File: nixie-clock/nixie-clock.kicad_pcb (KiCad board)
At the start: 2 copper layers, 184 x 112 mm, 61 parts, among them J1 Barrel_Jack_Switch, J2 Conn_01x08, J3 Conn_01x06, J4 AVR-ISP-6, SW1 SW_Push, SW2 SW_Push, SW3 SW_Push, SW4 SW_Push, U1 NCH6100HV, U10 74HC595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

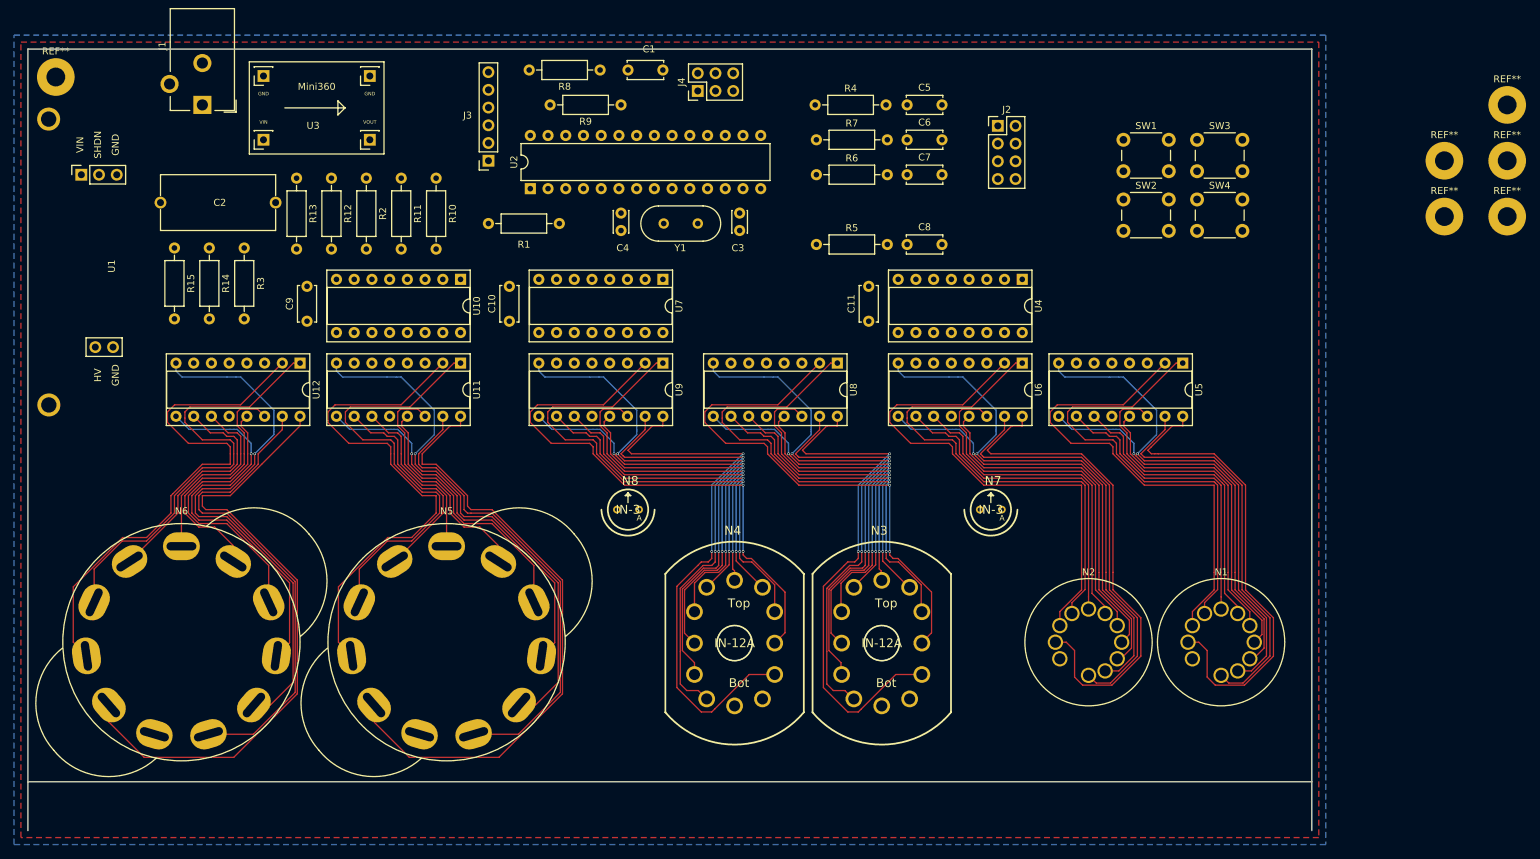
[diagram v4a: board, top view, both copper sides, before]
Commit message: Routed near microcontroller. Going to finish 74HC595-K155ID1 routing before returning to micro area.
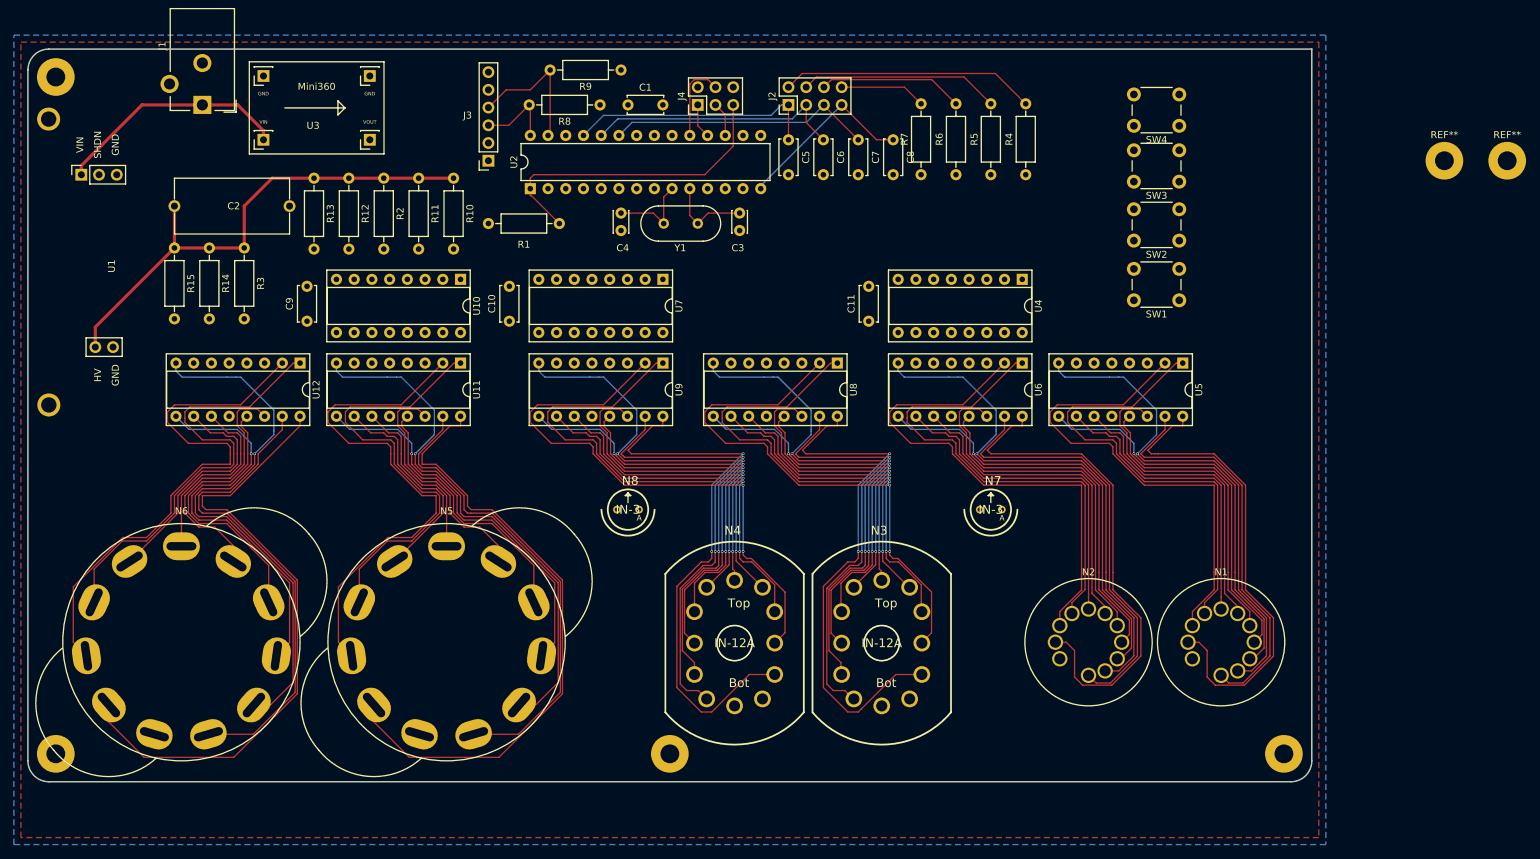
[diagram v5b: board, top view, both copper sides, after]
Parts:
- removed the REF** at (240.0, 38.0)
- removed the REF** at (231.0, 54.0)
- added REF**: MountingHole_2.7mm_M2.5_Pad, MountingHole:MountingHole_2.7mm_M2.5_Pad, F.Cu at (32.0, 131.0)
- added REF**: MountingHole_2.7mm_M2.5_Pad, MountingHole:MountingHole_2.7mm_M2.5_Pad, F.Cu at (120.0, 131.0)
- moved REF** 83.4 mm to (208.0, 131.0)
- moved R4 31.8 mm to (171.0, 48.0), turned to 90 degrees
- moved J2 30.1 mm to (137.0, 38.0), turned to 90 degrees
- moved R5 26.9 mm to (166.0, 48.0), turned to 90 degrees
- moved SW1 24.4 mm to (193.0, 66.0), turned to 180 degrees
- moved R6 20.0 mm to (161.0, 48.0), turned to 90 degrees
- moved C5 17.7 mm to (137.0, 43.0), turned to 270 degrees
- moved R7 15.8 mm to (156.0, 48.0), turned to 90 degrees
- moved C8 15.1 mm to (152.0, 43.0), turned to 270 degrees
- moved C6 12.0 mm to (142.0, 43.0), turned to 270 degrees
- moved SW4 10.9 mm to (193.0, 41.0), turned to 180 degrees
- moved SW2 9.94 mm to (193.0, 57.5), turned to 180 degrees
- moved C7 8.60 mm to (147.0, 43.0), turned to 270 degrees
- moved SW3 6.52 mm to (193.0, 49.0), turned to 180 degrees
- moved C1 5.00 mm to (119.0, 38.0)
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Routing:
- net +170V: track 0.00 -> 72.6 mm
- net SPI_RST: track 0.00 -> 45.2 mm
- net pb_plus: track 0.00 -> 38.2 mm
- net pb_minus: track 0.00 -> 37.2 mm
- net Net-(J2-Pad2): track 0.00 -> 36.6 mm
- net pb_programming_select: track 0.00 -> 36.2 mm
- net +12V: track 0.00 -> 33.9 mm
- net Net-(J2-Pad4): track 0.00 -> 28.7 mm
- net pb_display_on: track 0.00 -> 26.3 mm
- net Net-(J2-Pad6): track 0.00 -> 20.8 mm
- net SDA: track 0.00 -> 20.6 mm
- net Net-(J2-Pad8): track 0.00 -> 12.4 mm
- net XTAL2: track 0.00 -> 12.2 mm
- net XTAL1: track 0.00 -> 12.1 mm
- net SPI_MOSI: track 0.00 -> 11.8 mm
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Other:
- board size 184 x 112 mm -> 184 x 105 mm
- board text removed: "Arrange parts approximately Add edge cuts Add fills Rat race Pushbutton board"

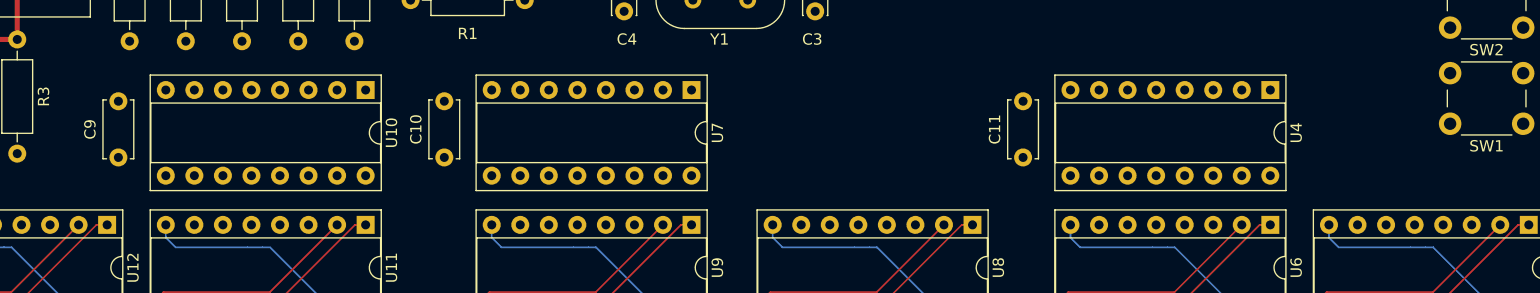
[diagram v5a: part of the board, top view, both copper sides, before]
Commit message: Finished seconds and minutes SR-K155ID1 exchange. Hours one is a bit different. Rotated SRs for better pin placement.
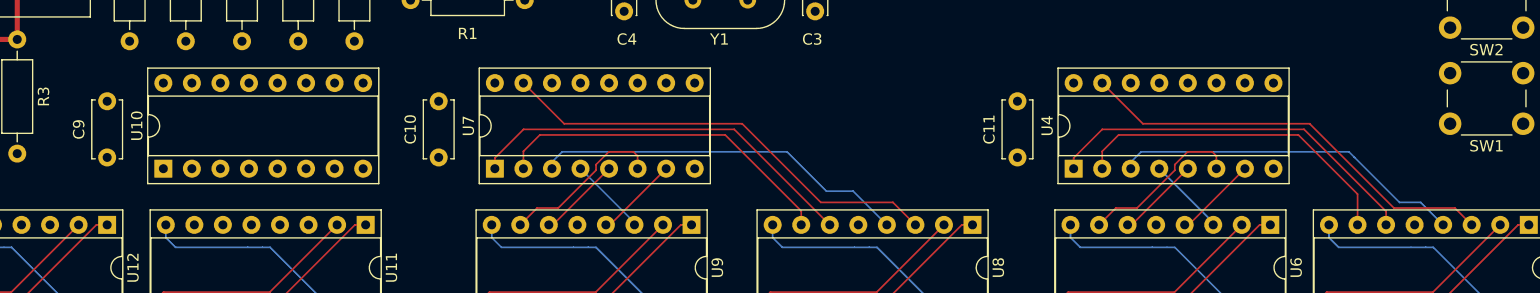
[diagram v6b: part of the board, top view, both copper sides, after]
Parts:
- moved U10 19.3 mm to (72.0, 70.0), turned to 90 degrees
- moved U4 18.8 mm to (153.0, 70.0), turned to 90 degrees
- moved U7 18.8 mm to (101.5, 70.0), turned to 90 degrees
- moved C9 1.00 mm to (67.0, 69.0)
- moved C10 0.50 mm to (96.5, 69.0)
- moved C11 0.50 mm to (148.0, 69.0)
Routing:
- net /shiftout/N3_A: track 0.00 -> 40.1 mm
- net /shiftout/N1_A: track 0.00 -> 38.1 mm
- net /shiftout/N3_B: track 0.00 -> 35.3 mm
- net /shiftout/N1_B: track 0.00 -> 34.0 mm
- net /shiftout/N3_D: track 0.00 -> 33.5 mm
- net /shiftout/N1_D: track 0.00 -> 31.5 mm
- net /shiftout/N3_C: track 0.00 -> 30.9 mm
- net /shiftout/N1_C: track 0.00 -> 29.8 mm
- net /shiftout/N4_C: track 0.00 -> 14.7 mm
- net /shiftout/N2_C: track 0.00 -> 14.7 mm
- net /shiftout/N2_D: track 0.00 -> 7.43 mm
- net /shiftout/N2_B: track 0.00 -> 7.43 mm
- net /shiftout/N4_D: track 0.00 -> 7.07 mm
- net /shiftout/N4_B: track 0.00 -> 7.07 mm
- net /shiftout/N2_A: track 0.00 -> 6.99 mm
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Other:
- board text added: "Anodes for all nixies Cross SR connections Extra pushbuttons Pushbutton mounting board Final board shape Extras (margins, info, symbols) on silkscreen"
- board text added: "This gap is off from the others. Did not catch the minor mistake before routing"

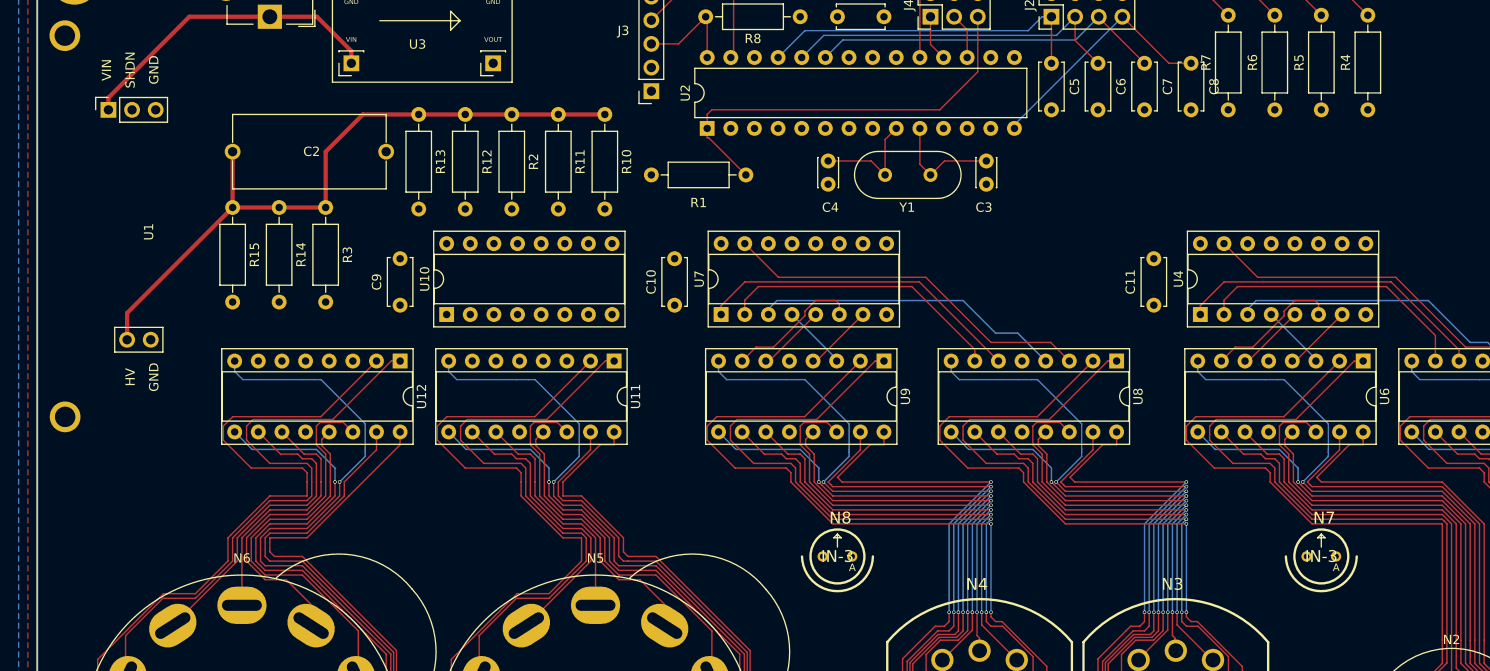
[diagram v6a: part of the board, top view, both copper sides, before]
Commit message: About to begin inter-74HC595 signals. Save point.
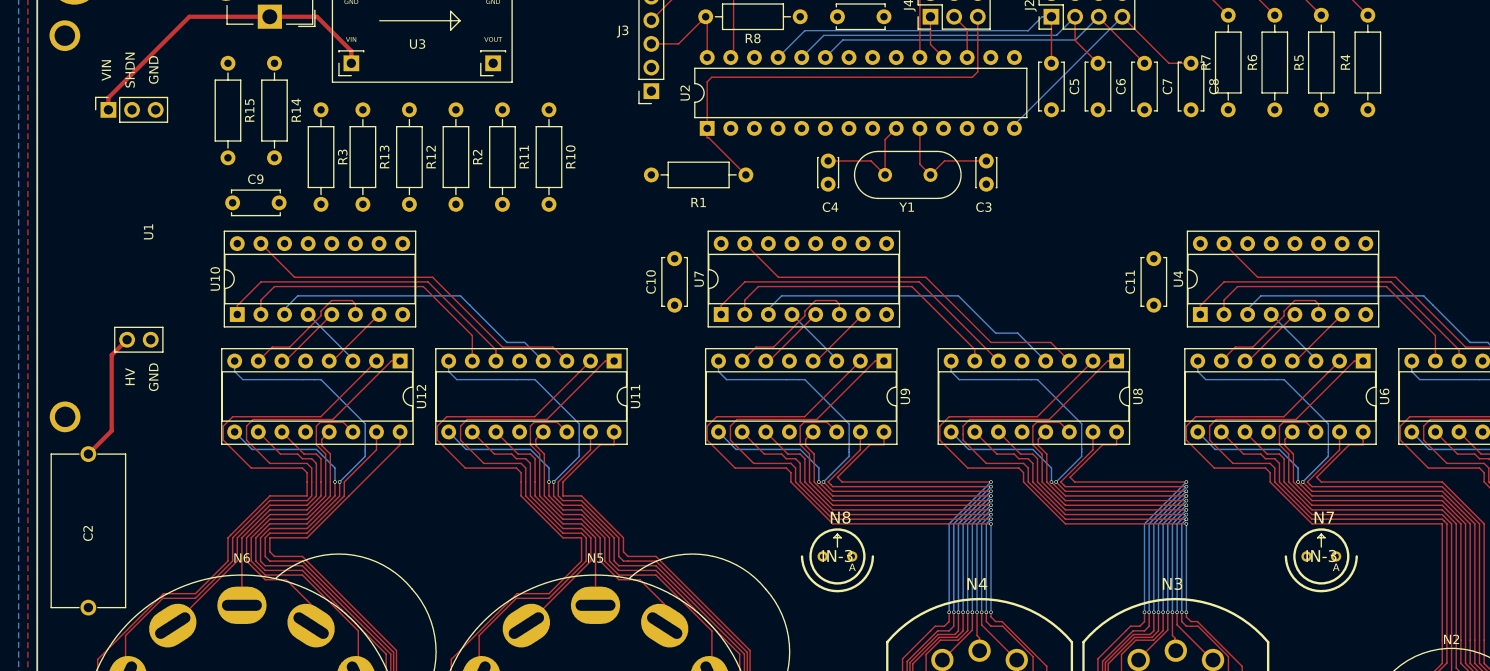
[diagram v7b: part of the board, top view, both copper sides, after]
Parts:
- moved C2 36.0 mm to (33.5, 85.0), turned to 270 degrees
- moved U10 22.5 mm to (49.5, 70.0)
- moved C9 21.1 mm to (49.0, 58.0), turned to 0 degrees
- moved R14 15.5 mm to (53.5, 43.0)
- moved R15 15.5 mm to (48.5, 43.0)
- moved R3 10.5 mm to (58.5, 48.0)
- moved R10 6.02 mm to (83.0, 48.0)
- moved R11 6.02 mm to (78.0, 48.0)
- moved R12 6.02 mm to (68.0, 48.0)
- moved R13 6.02 mm to (63.0, 48.0)
- moved R2 6.02 mm to (73.0, 48.0)
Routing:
- net +170V: track 72.6 -> 14.0 mm
- net /shiftout/N5_A: track 0.00 -> 38.1 mm
- net /shiftout/N5_B: track 0.00 -> 34.0 mm
- net /shiftout/N5_D: track 0.00 -> 31.9 mm
- net /shiftout/N5_C: track 0.00 -> 29.8 mm
- net /shiftout/N6_C: track 0.00 -> 14.7 mm
- net /shiftout/N6_D: track 0.00 -> 7.43 mm
- net /shiftout/N6_B: track 0.00 -> 7.07 mm
- net /shiftout/N6_A: track 0.00 -> 6.79 mm
- net SPI_RST: track 45.2 -> 47.3 mm

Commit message: Finished inter-74HC595 routing.
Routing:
- net SRCLK: track 0.00 -> 123.8 mm, vias 0 -> 2
- net SRLATCH: track 0.00 -> 123.0 mm, vias 0 -> 2
- net Net-(U10-Pad14): track 0.00 -> 68.8 mm
- net Net-(U4-Pad9): track 0.00 -> 68.3 mm
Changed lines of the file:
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@@
     (thickness 1.6)
     (drawings 36)
-    (tracks 1200)
+    (tracks 1246)
     (zones 0)
     (modules 61)
@@
   (gr_line (start 212 132) (end 212 30) (layer Edge.Cuts) (width 0.2))
   (gr_line (start 31 135) (end 209 135) (layer Edge.Cuts) (width 0.2))
+  (segment (start 111.66 59.66) (end 111.5 59.5) (width 0.1524) (layer F.Cu) (net 39))
+  (segment (start 111.5 59.5) (end 111.5 59.5) (width 0.1524) (layer F.Cu) (net 39))
+  (via (at 111.5 59.5) (size 0.381) (drill 0.254) (layers F.Cu B.Cu) (net 39))
+  (segment (start 111.66 61.34) (end 111.66 62.38) (width 0.1524) (layer F.Cu) (net 39))
+  (segment (start 111.66 61.34) (end 111.66 59.66) (width 0.1524) (layer F.Cu) (net 39))
+  (segment (start 114.2 60.2) (end 114 60) (width 0.1524) (layer F.Cu) (net 40))
+  (segment (start 114.2 62.38) (end 114.2 60.2) (width 0.1524) (layer F.Cu) (net 40))
+  (via (at 114 60) (size 0.381) (drill 0.254) (layers F.Cu B.Cu) (net 40))
+  (segment (start 114 60) (end 114 60) (width 0.1524) (layer F.Cu) (net 40))
+  (via (at 163 59.5) (size 0.381) (drill 0.254) (layers F.Cu B.Cu) (net 39))
+  (segment (start 163.16 59.66) (end 163 59.5) (width 0.1524) (layer F.Cu) (net 39))
+  (segment (start 163 59.5) (end 163 59.5) (width 0.1524) (layer F.Cu) (net 39))
+  (segment (start 165.5 60) (end 165.5 60) (width 0.1524) (layer F.Cu) (net 40))
+  (segment (start 165.5 60) (end 160.5 60) (width 0.1524) (layer B.Cu) (net 40))
+  (via (at 165.5 60) (size 0.381) (drill 0.254) (layers F.Cu B.Cu) (net 40))
   (segment (start 33.5 85) (end 36 82.5) (width 0.4572) (layer F.Cu) (net 3))
   (segment (start 36 74.37) (end 37.66 72.71) (width 0.4572) (layer F.Cu) (net 3))
@@
   (segment (start 124 40.98) (end 124 38) (width 0.1524) (layer F.Cu) (net 22))
   (segment (start 125.4 42.38) (end 124 40.98) (width 0.1524) (layer F.Cu) (net 22))
+  (segment (start 163.16 61.34) (end 163.16 62.38) (width 0.1524) (layer F.Cu) (net 39))
+  (segment (start 163.16 61.88) (end 163.16 61.34) (width 0.1524) (layer F.Cu) (net 39))
+  (segment (start 163.16 61.34) (end 163.16 59.66) (width 0.1524) (layer F.Cu) (net 39))
+  (segment (start 163 59.5) (end 160.5 59.5) (width 0.1524) (layer B.Cu) (net 39))
+  (segment (start 160.5 59.5) (end 111.5 59.5) (width 0.1524) (layer B.Cu) (net 39))
+  (segment (start 61 59.5) (end 59.66 60.84) (width 0.1524) (layer B.Cu) (net 39))
+  (segment (start 59.66 60.84) (end 59.66 62.38) (width 0.1524) (layer B.Cu) (net 39))
+  (segment (start 111.5 59.5) (end 61 59.5) (width 0.1524) (layer B.Cu) (net 39))
+  (segment (start 111.5 53.88) (end 111.5 59.5) (width 0.1524) (layer B.Cu) (net 39))
+  (segment (start 107.62 50) (end 111.5 53.88) (width 0.1524) (layer B.Cu) (net 39))
+  (segment (start 165.7 60.2) (end 165.5 60) (width 0.1524) (layer F.Cu) (net 40))
+  (segment (start 165.7 62.38) (end 165.7 60.2) (width 0.1524) (layer F.Cu) (net 40))
+  (segment (start 114 60) (end 160.5 60) (width 0.1524) (layer B.Cu) (net 40))
+  (segment (start 63 60) (end 109 60) (width 0.1524) (layer B.Cu) (net 40))
+  (segment (start 109 60) (end 114 60) (width 0.1524) (layer B.Cu) (net 40))
+  (segment (start 62.2 60.8) (end 63 60) (width 0.1524) (layer B.Cu) (net 40))
+  (segment (start 62.2 62.38) (end 62.2 60.8) (width 0.1524) (layer B.Cu) (net 40))
+  (segment (start 105.879999 50.799999) (end 105.879999 51.879999) (width 0.1524) (layer F.Cu) (net 40))
+  (segment (start 106.5 52.5) (end 114 60) (width 0.1524) (layer F.Cu) (net 40))
+  (segment (start 105.879999 51.879999) (end 106.5 52.5) (width 0.1524) (layer F.Cu) (net 40))
+  (segment (start 105.08 50) (end 105.879999 50.799999) (width 0.1524) (layer F.Cu) (net 40))
+  (segment (start 123.5 65.5) (end 109.7 65.5) (width 0.1524) (layer B.Cu) (net 44))
+  (segment (start 168.9 60.5) (end 128.5 60.5) (width 0.1524) (layer B.Cu) (net 44))
+  (segment (start 109.7 65.5) (end 106.58 62.38) (width 0.1524) (layer B.Cu) (net 44))
+  (segment (start 128.5 60.5) (end 123.5 65.5) (width 0.1524) (layer B.Cu) (net 44))
+  (segment (start 170.78 62.38) (end 168.9 60.5) (width 0.1524) (layer B.Cu) (net 44))
+  (segment (start 57.7 65.5) (end 54.58 62.38) (width 0.1524) (layer B.Cu) (net 45))
+  (segment (start 70.5 65.5) (end 57.7 65.5) (width 0.1524) (layer B.Cu) (net 45))
+  (segment (start 75.5 60.5) (end 70.5 65.5) (width 0.1524) (layer B.Cu) (net 45))
+  (segment (start 117.4 60.5) (end 75.5 60.5) (width 0.1524) (layer B.Cu) (net 45))
+  (segment (start 119.28 62.38) (end 117.4 60.5) (width 0.1524) (layer B.Cu) (net 45))
   (segment (start 138.5 88.5) (end 151.5 88.5) (width 0.1524) (layer F.Cu) (net 75))
   (segment (start 138.5 89) (end 151.5 89) (width 0.1524) (layer F.Cu) (net 74))
